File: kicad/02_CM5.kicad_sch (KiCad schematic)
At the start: 0 parts

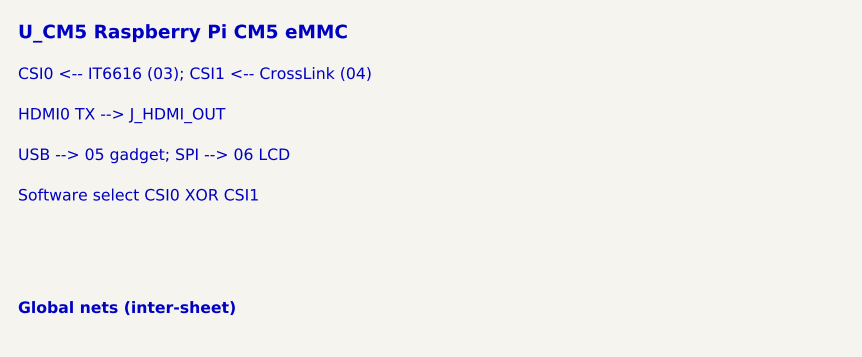
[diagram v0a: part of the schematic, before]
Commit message: Add Antmicro SDI ingest sheet and real SDI playback out.
Import GS2971A+CrossLink into sheet 04, require GS2962A playback path (not input loop), and lock IT6616 HDMI CSI.

Co-authored-by: Cursor <cursoragent@cursor.com>
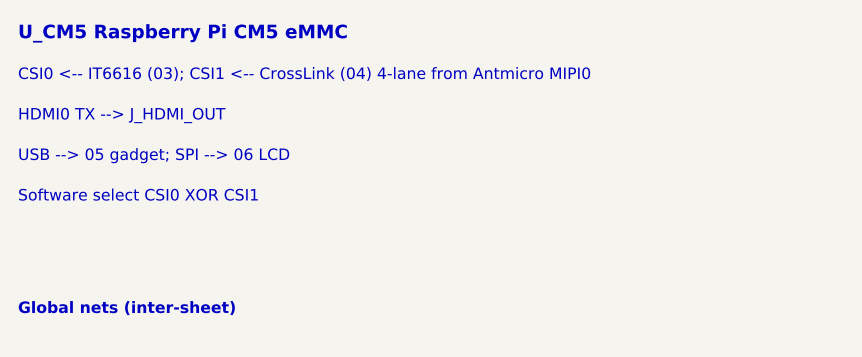
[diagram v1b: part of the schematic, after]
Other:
- note added: "CSI0 <-- IT6616 (03); CSI1 <-- CrossLink (04) 4-lane from Antmicro MIPI0"
- note removed: "CSI0 <-- IT6616 (03); CSI1 <-- CrossLink (04)"
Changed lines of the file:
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@@
     (effects (font (size 1.5 1.5) (bold yes)) (justify left bottom))
   )
-  (text "CSI0 <-- IT6616 (03); CSI1 <-- CrossLink (04)"
+  (text "CSI0 <-- IT6616 (03); CSI1 <-- CrossLink (04) 4-lane from Antmicro MIPI0"
     (exclude_from_sim no)
     (at 25 22.5 0)

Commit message: Wire sheet 07 SDI playback path with real symbols.
Add IT66021FN and GS2962A library symbols, TMDS 1:2 buffer to HDMI monitor and SDI out, and expand CM5 HDMI TMDS nets.

Co-authored-by: Cursor <cursoragent@cursor.com>
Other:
- note added: "HDMI0 TX (HDMI_TX_D0/D1/D2/CK P/N) --> sheet 07 TMDS buffer / monitor / SDI"
- note removed: "HDMI0 TX --> J_HDMI_OUT"
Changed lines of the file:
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@@
     (effects (font (size 1.27 1.27)) (justify left bottom))
   )
-  (text "HDMI0 TX --> J_HDMI_OUT"
+  (text "HDMI0 TX (HDMI_TX_D0/D1/D2/CK P/N) --> sheet 07 TMDS buffer / monitor / SDI"
     (exclude_from_sim no)
     (at 25 27.0 0)
@@
       (effects (font (size 1.27 1.27)) (hide yes))
     )
+  )
+  (global_label "HDMI_TX_D0_P"
+    (shape output)
+    (at 25 144.5 0)
+    (effects (font (size 1.27 1.27)) (justify left))
+    (fields_autoplaced yes)
+    (property "Intersheetrefs" "${INTERSHEET_REFS}" (at 25 144.5 0)
+      (effects (font (size 1.27 1.27)) (hide yes))
+    )
+  )
+  (global_label "HDMI_TX_D0_N"
+    (shape output)
+    (at 25 149.5 0)
+    (effects (font (size 1.27 1.27)) (justify left))
+    (fields_autoplaced yes)
+    (property "Intersheetrefs" "${INTERSHEET_REFS}" (at 25 149.5 0)
+      (effects (font (size 1.27 1.27)) (hide yes))
+    )
+  )
+  (global_label "HDMI_TX_D1_P"
+    (shape output)
+    (at 25 154.5 0)
+    (effects (font (size 1.27 1.27)) (justify left))
+    (fields_autoplaced yes)
+    (property "Intersheetrefs" "${INTERSHEET_REFS}" (at 25 154.5 0)
+      (effects (font (size 1.27 1.27)) (hide yes))
+    )
+  )
+  (global_label "HDMI_TX_D1_N"
+    (shape output)
+    (at 25 159.5 0)
+    (effects (font (size 1.27 1.27)) (justify left))
+    (fields_autoplaced yes)
+    (property "Intersheetrefs" "${INTERSHEET_REFS}" (at 25 159.5 0)
+      (effects (font (size 1.27 1.27)) (hide yes))
+    )
+  )
+  (global_label "HDMI_TX_D2_P"
+    (shape output)
+    (at 25 164.5 0)
+    (effects (font (size 1.27 1.27)) (justify left))
+    (fields_autoplaced yes)
+    (property "Intersheetrefs" "${INTERSHEET_REFS}" (at 25 164.5 0)
+      (effects (font (size 1.27 1.27)) (hide yes))
+    )
+  )
+  (global_label "HDMI_TX_D2_N"
+    (shape output)
+    (at 25 169.5 0)
+    (effects (font (size 1.27 1.27)) (justify left))
+    (fields_autoplaced yes)
+    (property "Intersheetrefs" "${INTERSHEET_REFS}" (at 25 169.5 0)
+      (effects (font (size 1.27 1.27)) (hide yes))
+    )
+  )
+  (global_label "HDMI_TX_CK_P"
+    (shape output)
+    (at 25 174.5 0)
+    (effects (font (size 1.27 1.27)) (justify left))
+    (fields_autoplaced yes)
+    (property "Intersheetrefs" "${INTERSHEET_REFS}" (at 25 174.5 0)
+      (effects (font (size 1.27 1.27)) (hide yes))
+    )
+  )
+  (global_label "HDMI_TX_CK_N"
+    (shape output)
+    (at 25 179.5 0)
+    (effects (font (size 1.27 1.27)) (justify left))
+    (fields_autoplaced yes)
+    (property "Intersheetrefs" "${INTERSHEET_REFS}" (at 25 179.5 0)
+      (effects (font (size 1.27 1.27)) (hide yes))
+    )
+  )
+  (global_label "SDI_TX_SPI_MOSI"
+    (shape output)
+    (at 25 184.5 0)
+    (effects (font (size 1.27 1.27)) (justify left))
+    (fields_autoplaced yes)
+    (property "Intersheetrefs" "${INTERSHEET_REFS}" (at 25 184.5 0)
+      (effects (font (size 1.27 1.27)) (hide yes))
+    )
+  )
+  (global_label "SDI_TX_SPI_MISO"
+    (shape input)
+    (at 25 189.5 0)
+    (effects (font (size 1.27 1.27)) (justify left))
+    (fields_autoplaced yes)
+    (property "Intersheetrefs" "${INTERSHEET_REFS}" (at 25 189.5 0)
+      (effects (font (size 1.27 1.27)) (hide yes))
+    )
+  )
+  (global_label "SDI_TX_SPI_SCK"
+    (shape output)
+    (at 25 194.5 0)
+    (effects (font (size 1.27 1.27)) (justify left))
+    (fields_autoplaced yes)
+    (property "Intersheetrefs" "${INTERSHEET_REFS}" (at 25 194.5 0)
+      (effects (font (size 1.27 1.27)) (hide yes))
+    )
+  )
+  (global_label "SDI_TX_SPI_CS"
+    (shape output)
+    (at 25 199.5 0)
+    (effects (font (size 1.27 1.27)) (justify left))
+    (fields_autoplaced yes)
+    (property "Intersheetrefs" "${INTERSHEET_REFS}" (at 25 199.5 0)
+      (effects (font (size 1.27 1.27)) (hide yes))
+    )
